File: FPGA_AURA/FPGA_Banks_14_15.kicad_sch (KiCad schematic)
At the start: 22 parts, among them U1 XC7A35T-2FTG256C, Y500 ASEM1-100.000MHZ-LC-T

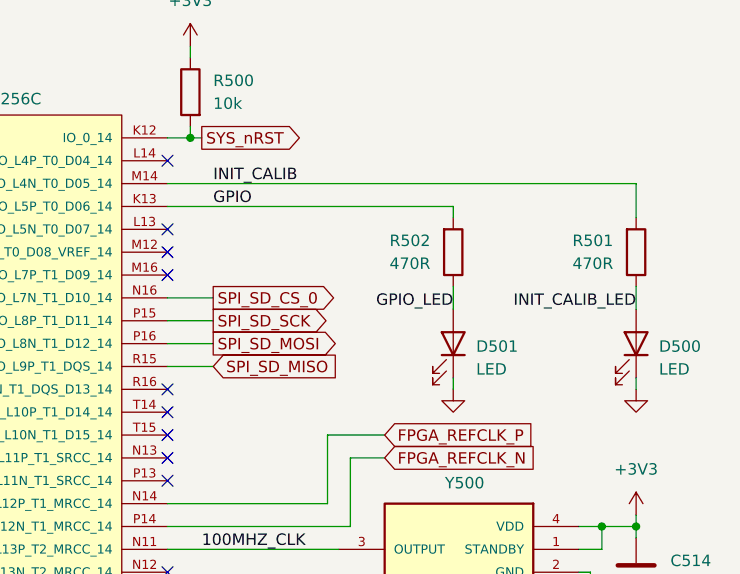
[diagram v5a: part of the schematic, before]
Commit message: Schematic initial draft complete.
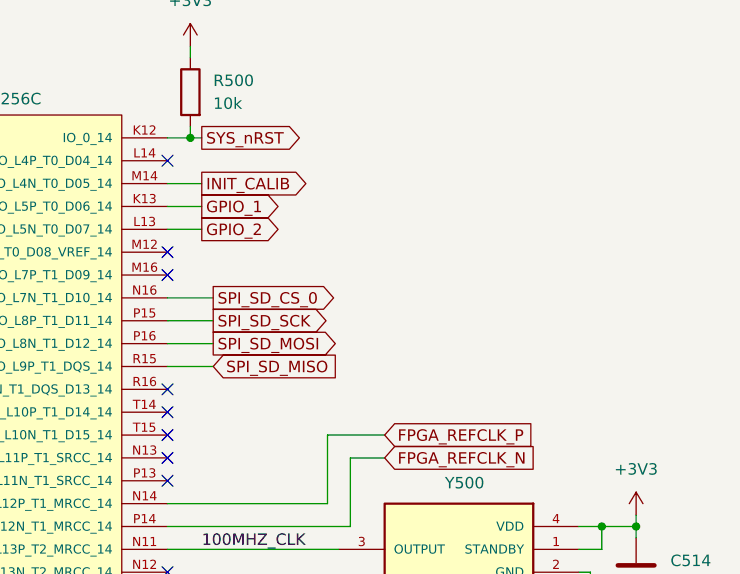
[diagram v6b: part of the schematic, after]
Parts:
- removed D500, D501: LED, LED_SMD:LED_0603_1608Metric, symbol Device:LED
- removed R501, R502: 470R, Resistor_SMD:R_0402_1005Metric, symbol Device:R
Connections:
- net GPIO_2: now reaches U1.L13 (IO_L5N_T0_D07_14)
- net GPIO renamed GPIO_1
- no-connect marks 20 -> 19

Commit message: Continued routing and pin swapping, 11 nets left to route.
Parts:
- removed R500: 10k, Resistor_SMD:R_0402_1005Metric, symbol Device:R
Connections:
- net CAN_TX: now also U1.P6 (IO_25_14); no longer U1.N6 (IO_L19N_T3_A09_D25_VREF_14)
- net SPI_3V3_CS_2: now also U1.N6 (IO_L19N_T3_A09_D25_VREF_14); no longer U1.N9 (IO_L18P_T2_A12_D28_14)
- net SYS_nRST: no longer names the net of U1.K12 (IO_0_14)
- no-connect marks 19 -> 20
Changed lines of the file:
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@@
 	)
 	(junction
-		(at 224.79 45.72)
-		(diameter 0)
-		(color 0 0 0 0)
-	)
-	(junction
 		(at 163.83 59.69)
 		(diameter 0)
@@
 	)
 	(no_connect
+		(at 222.25 114.3)
+	)
+	(no_connect
 		(at 222.25 134.62)
 	)
 	(no_connect
+		(at 222.25 45.72)
+	)
+	(no_connect
 		(at 222.25 48.26)
 	)
@@
 	)
 	(no_connect
-		(at 222.25 149.86)
-	)
-	(no_connect
 		(at 222.25 96.52)
 	)
 	(wire
 		(pts
-			(xy 226.06 121.92) (xy 222.25 121.92)
+			(xy 99.06 88.9) (xy 99.06 90.17)
 		)
 		(stroke
@@
 	(wire
 		(pts
-			(xy 99.06 88.9) (xy 99.06 90.17)
+			(xy 222.25 149.86) (xy 226.06 149.86)
 		)
 		(stroke
@@
 	(wire
 		(pts
-			(xy 226.06 114.3) (xy 222.25 114.3)
-		)
-		(stroke
-			(width 0)
-			(type default)
-		)
-	)
-	(wire
-		(pts
 			(xy 270.51 88.9) (xy 267.97 88.9)
 		)
@@
 	(wire
 		(pts
+			(xy 222.25 121.92) (xy 226.06 121.92)
+		)
+		(stroke
+			(width 0)
+			(type default)
+		)
+	)
+	(wire
+		(pts
 			(xy 40.64 45.72) (xy 36.83 45.72)
 		)
@@
 	(wire
 		(pts
-			(xy 224.79 44.45) (xy 224.79 45.72)
-		)
-		(stroke
-			(width 0)
-			(type default)
-		)
-	)
-	(wire
-		(pts
 			(xy 40.64 129.54) (xy 36.83 129.54)
 		)
@@
 	(wire
 		(pts
-			(xy 224.79 35.56) (xy 224.79 36.83)
-		)
-		(stroke
-			(width 0)
-			(type default)
-		)
-	)
-	(wire
-		(pts
 			(xy 226.06 144.78) (xy 222.25 144.78)
 		)
@@
 	(wire
 		(pts
-			(xy 226.06 45.72) (xy 224.79 45.72)
-		)
-		(stroke
-			(width 0)
-			(type default)
-		)
-	)
-	(wire
-		(pts
 			(xy 99.06 60.96) (xy 87.63 60.96)
 		)
@@
 	(wire
 		(pts
-			(xy 224.79 45.72) (xy 222.25 45.72)
-		)
-		(stroke
-			(width 0)
-			(type default)
-		)
-	)
-	(wire
-		(pts
 			(xy 138.43 59.69) (xy 151.13 59.69)
 		)
@@
 		)
 	)
-	(global_label "SYS_nRST"
-		(shape output)
-		(at 226.06 45.72 0)
-		(fields_autoplaced yes)
-		(effects
-			(font
-				(size 1.27 1.27)
-			)
-			(justify left)
-		)
-		(property "Intersheetrefs" "${INTERSHEET_REFS}"
-			(at 238.1165 45.72 0)
-			(hide yes)
-			(show_name no)
-			(do_not_autoplace no)
-			(effects
-				(font
-					(size 1.27 1.27)
-				)
-				(justify left)
-			)
-		)
-	)
 	(global_label "SPI_SD_SCK"
 		(shape output)
@@
 	(global_label "SPI_3V3_CS_2"
 		(shape output)
-		(at 226.06 114.3 0)
+		(at 226.06 121.92 0)
 		(fields_autoplaced yes)
 		(effects
@@
 		)
 		(property "Intersheetrefs" "${INTERSHEET_REFS}"
-			(at 242.2289 114.3 0)
+			(at 242.2289 121.92 0)
 			(hide yes)
 			(show_name no)
@@
 	(global_label "CAN_TX"
 		(shape output)
-		(at 226.06 121.92 0)
+		(at 226.06 149.86 0)
 		(fields_autoplaced yes)
 		(effects
@@
 		)
 		(property "Intersheetrefs" "${INTERSHEET_REFS}"
-			(at 235.879 121.92 0)
+			(at 235.879 149.86 0)
 			(hide yes)
 			(show_name no)
@@
 	)
 	(symbol
-		(lib_id "Device:R")
-		(at 224.79 40.64 0)
-		(mirror y)
-		(unit 1)
-		(body_style 1)
-		(exclude_from_sim no)
-		(in_bom yes)
-		(on_board yes)
-		(in_pos_files yes)
-		(dnp no)
-		(fields_autoplaced yes)
-		(property "Reference" "R500"
-			(at 227.33 39.3699 0)
-			(show_name no)
-			(do_not_autoplace no)
-			(effects
-				(font
-					(size 1.27 1.27)
-				)
-				(justify right)
-			)
-		)
-		(property "Value" "10k"
-			(at 227.33 41.9099 0)
-			(show_name no)
-			(do_not_autoplace no)
-			(effects
-				(font
-					(size 1.27 1.27)
-				)
-				(justify right)
-			)
-		)
-		(property "Footprint" "Resistor_SMD:R_0402_1005Metric"
-			(at 226.568 40.64 90)
-			(hide yes)
-			(show_name no)
-			(do_not_autoplace no)
-			(effects
-				(font
-					(size 1.27 1.27)
-				)
-			)
-		)
-		(property "Datasheet" ""
-			(at 224.79 40.64 0)
-			(hide yes)
-			(show_name no)
-			(do_not_autoplace no)
-			(effects
-				(font
-					(size 1.27 1.27)
-				)
-			)
-		)
-		(property "Description" "Resistor"
-			(at 224.79 40.64 0)
-			(hide yes)
-			(show_name no)
-			(do_not_autoplace no)
-			(effects
-				(font
-					(size 1.27 1.27)
-				)
-			)
-		)
-		(pin "2"
-		)
-		(pin "1"
-		)
-		(instances
-			(project "FPGA_AURA"
-				(path "/3d83cb23-9528-4d06-8969-599520e9eb23/49fa5711-315f-4731-8075-f443e3d2a01c"
-					(reference "R500")
-					(unit 1)
-				)
-			)
-		)
-	)
-	(symbol
 		(lib_id "Device:C")
 		(at 111.76 85.09 0)
@@
 					(unit 1)
 				)
-			)
-		)
-	)
-	(symbol
-		(lib_id "power:+5V")
-		(at 224.79 35.56 0)
-		(mirror y)
-		(unit 1)
-		(body_style 1)
-		(exclude_from_sim no)
-		(in_bom yes)
-		(on_board yes)
-		(in_pos_files yes)
-		(dnp no)
-		(fields_autoplaced yes)
-		(property "Reference" "#PWR045"
-			(at 224.79 39.37 0)
-			(hide yes)
-			(show_name no)
-			(do_not_autoplace no)
-			(effects
-				(font
-					(size 1.27 1.27)
-				)
-			)
-		)
-		(property "Value" "+3V3"
-			(at 224.79 30.48 0)
-			(show_name no)
-			(do_not_autoplace no)
-			(effects
-				(font
-					(size 1.27 1.27)
-				)
-			)
-		)
-		(property "Footprint" ""
-			(at 224.79 35.56 0)
-			(hide yes)
-			(show_name no)
-			(do_not_autoplace no)
-			(effects
-				(font
-					(size 1.27 1.27)
-				)
-			)
-		)
-		(property "Datasheet" ""
-			(at 224.79 35.56 0)
-			(hide yes)
-			(show_name no)
-			(do_not_autoplace no)
-			(effects
-				(font
-					(size 1.27 1.27)
-				)
-			)
-		)
-		(property "Description" "Power symbol creates a global label with name \"+5V\""
-			(at 224.79 35.56 0)
-			(hide yes)
-			(show_name no)
-			(do_not_autoplace no)
-			(effects
-				(font
-					(size 1.27 1.27)
-				)
-			)
-		)
-		(pin "1"
-		)
-		(instances
-			(project "FPGA_AURA"
-				(path "/3d83cb23-9528-4d06-8969-599520e9eb23/49fa5711-315f-4731-8075-f443e3d2a01c"
-					(reference "#PWR045")
-					(unit 1)
-				)

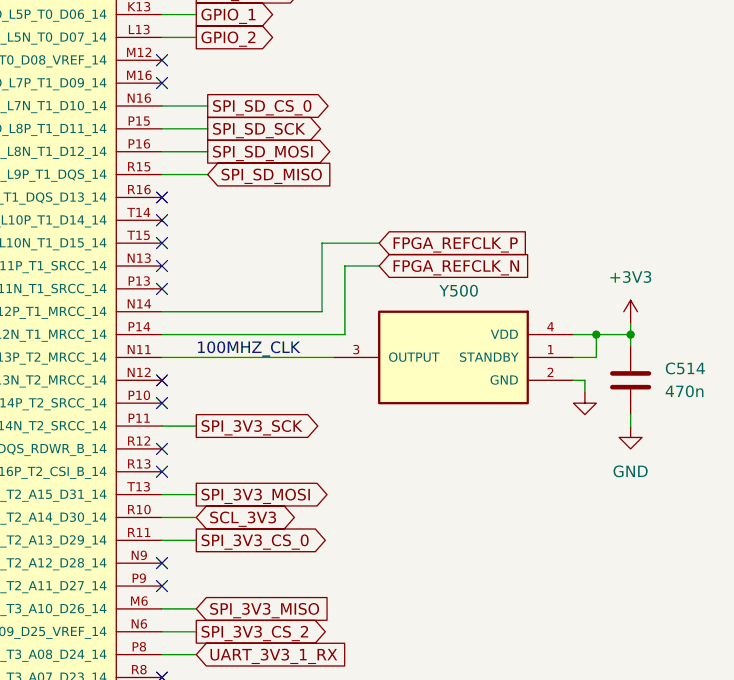
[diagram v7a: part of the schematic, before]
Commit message: Ready to order. Gerbers exported, delay matching checked, BoM made, manufacturing information added.
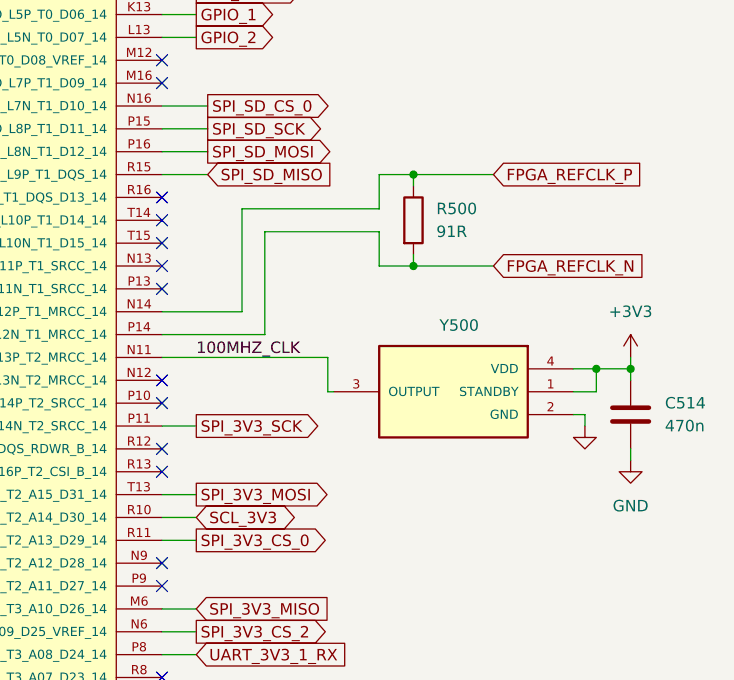
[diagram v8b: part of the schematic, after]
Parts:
- added R500: 91R, Resistor_SMD:R_0201_0603Metric, symbol Device:R
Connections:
- net FPGA_REFCLK_N: now also R500.2
- net FPGA_REFCLK_P: now also R500.1
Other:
- moved on the sheet: C514, Y500
